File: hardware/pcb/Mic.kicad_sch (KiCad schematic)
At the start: 4 parts

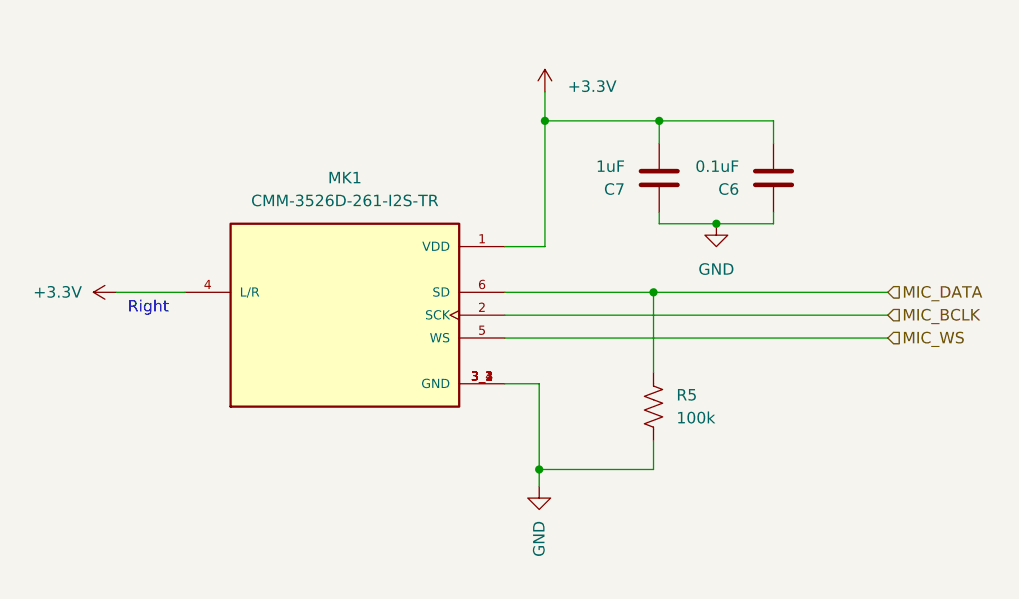
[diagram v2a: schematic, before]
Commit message: Replace EOL CUI devices microphone with Knowles SPH0645
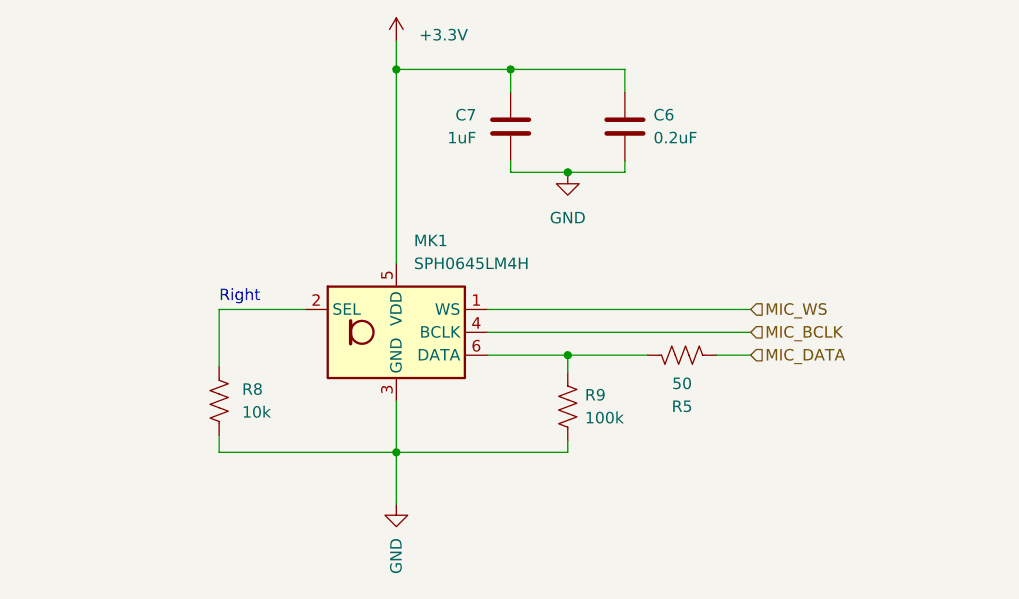
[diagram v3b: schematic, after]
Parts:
- removed MK1: CMM-3526D-261-I2S-TR, CMM-3526D-261-I2S-TR:MIC_CMM-3526D-261-I2S-TR, symbol CMM-3526D-261-I2S-TR:CMM-3526D-261-I2S-TR
- added MK1: SPH0645LM4H, Sensor_Audio:Knowles_SPH0645LM4H-6_3.5x2.65mm, symbol Sensor_Audio:SPH0645LM4H
- added R8: 10k, Resistor_SMD:R_1206_3216Metric_Pad1.30x1.75mm_HandSolder, symbol Device:R_US
- added R9: 100k, Resistor_SMD:R_1206_3216Metric_Pad1.30x1.75mm_HandSolder, symbol Device:R_US
- C6: value 0.1uF -> 0.2uF
- R5: value 100k -> 50
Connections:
- net +3.3V: now also MK1.5 (VDD)
- net GND: now also MK1.3 (GND), R8.2, R9.2; no longer R5.2
- net MIC_BCLK: now also MK1.4 (BCLK)
- net MIC_DATA: now also R5.2; no longer R5.1
- net MIC_WS: now also MK1.1 (WS)
- new net: MK1.6 (DATA), R5.1, R9.1
- new net: MK1.2 (SEL), R8.1
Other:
- moved on the sheet: C6, C7, R5
